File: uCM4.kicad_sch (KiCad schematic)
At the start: 63 parts, among them J1 UART, J10 Conn_01x04, J11 GPS, J2 Micro_SD_Card_Det, J3 I2C1, J4 USB_B_Micro, J5 DummyJ, J6 DummyJ, J7 SolderJumper_2_Open, J8 Camera 0, J9 Camera 1, SW1 SW_DIP_x01, SW2 SW_DIP_x01, SW3 SW_Push, SW4 SW_Push, U1 BNO055, U18 RT9742GGJ5, U2 SN74LVC1G07DBVR, U3 TPD4EUSB30DQAR, U4 TPS61022

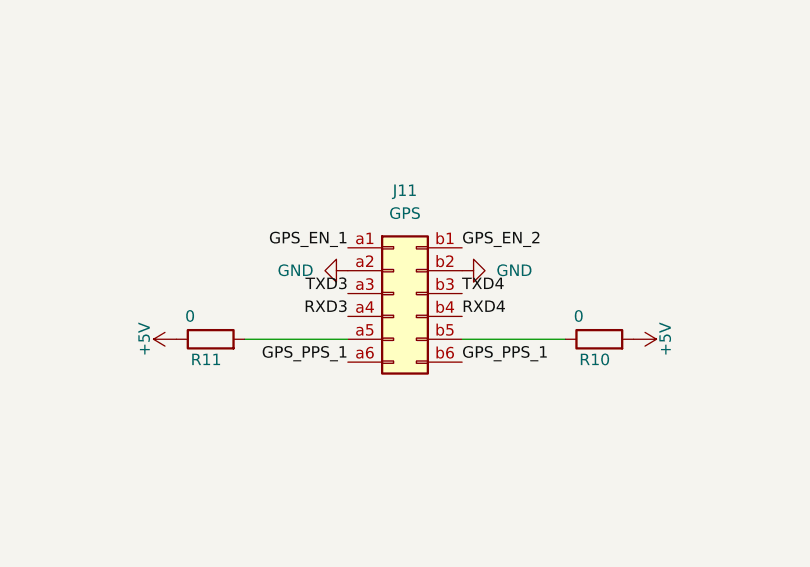
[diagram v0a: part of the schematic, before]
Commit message: Adding 3d models and arranging board
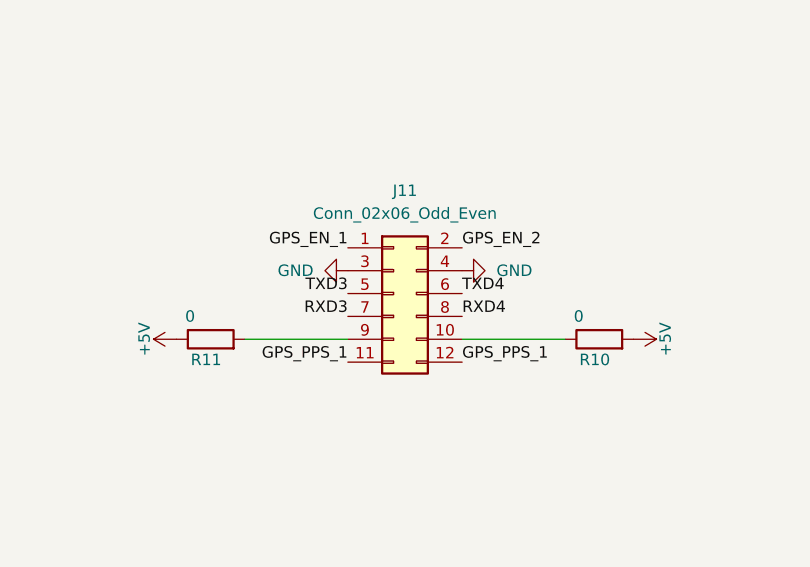
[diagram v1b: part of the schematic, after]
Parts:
- removed J11: GPS, symbol Connector_Generic:Conn_02x06_Row_Letter_First
- added J11: Conn_02x06_Odd_Even, Connector_PinHeader_2.54mm:PinHeader_2x06_P2.54mm_Vertical, symbol Connector_Generic:Conn_02x06_Odd_Even
- L1: footprint (none) -> CM4:XAL7030102MEC
- R19: footprint (none) -> Resistor_SMD:R_0603_1608Metric
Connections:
- net GND: now also J11.3 (Pin_3), J11.4 (Pin_4)
- net GPS_EN_1: now also J11.1 (Pin_1)
- net GPS_EN_2: now also J11.2 (Pin_2)
- net GPS_PPS_1: now also J11.11 (Pin_11), J11.12 (Pin_12)
- net RXD3: now also J11.7 (Pin_7)
- net RXD4: now also J11.8 (Pin_8)
- net TXD3: now also J11.5 (Pin_5)
- net TXD4: now also J11.6 (Pin_6)
- net at R11.2: now also J11.9 (Pin_9)
- net at R10.1: now also J11.10 (Pin_10)
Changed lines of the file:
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@@
 	)
 	(symbol
+		(lib_id "Connector_Generic:Conn_02x06_Odd_Even")
+		(at 162.56 64.77 0)
+		(unit 1)
+		(exclude_from_sim no)
+		(in_bom yes)
+		(on_board yes)
+		(dnp no)
+		(fields_autoplaced yes)
+		(property "Reference" "J11"
+			(at 163.83 53.34 0)
+			(effects
+				(font
+					(size 1.27 1.27)
+				)
+			)
+		)
+		(property "Value" "Conn_02x06_Odd_Even"
+			(at 163.83 55.88 0)
+			(effects
+				(font
+					(size 1.27 1.27)
+				)
+			)
+		)
+		(property "Footprint" "Connector_PinHeader_2.54mm:PinHeader_2x06_P2.54mm_Vertical"
+			(at 162.56 64.77 0)
+			(effects
+				(font
+					(size 1.27 1.27)
+				)
+				(hide yes)
+			)
+		)
+		(property "Datasheet" "~"
+			(at 162.56 64.77 0)
+			(effects
+				(font
+					(size 1.27 1.27)
+				)
+				(hide yes)
+			)
+		)
+		(property "Description" "Generic connector, double row, 02x06, odd/even pin numbering scheme (row 1 odd numbers, row 2 even numbers), script generated (kicad-library-utils/schlib/autogen/connector/)"
+			(at 162.56 64.77 0)
+			(effects
+				(font
+					(size 1.27 1.27)
+				)
+				(hide yes)
+			)
+		)
+		(pin "8"
+		)
+		(pin "5"
+		)
+		(pin "12"
+		)
+		(pin "4"
+		)
+		(pin "3"
+		)
+		(pin "1"
+		)
+		(pin "9"
+		)
+		(pin "6"
+		)
+		(pin "10"
+		)
+		(pin "7"
+		)
+		(pin "2"
+		)
+		(pin "11"
+		)
+		(instances
+			(project ""
+				(path "/ab308ddb-f5b4-4376-8062-4d719b3e690f"
+					(reference "J11")
+					(unit 1)
+				)
+			)
+		)
+	)
+	(symbol
 		(lib_id "power:GND")
 		(at 34.29 60.96 270)
@@
 			)
 		)
-		(property "Footprint" ""
+		(property "Footprint" "CM4:XAL7030102MEC"
 			(at 365.76 142.24 0)
 			(effects
@@
 			)
 		)
-		(property "Footprint" ""
+		(property "Footprint" "Resistor_SMD:R_0603_1608Metric"
 			(at 388.62 154.178 90)
 			(effects
@@
 					(unit 1)
 				)
-			)
-		)
-	)
-	(symbol
-		(lib_id "Connector_Generic:Conn_02x06_Row_Letter_First")
-		(at 162.56 64.77 0)
-		(unit 1)
-		(exclude_from_sim no)
-		(in_bom yes)
-		(on_board yes)
-		(dnp no)
-		(fields_autoplaced yes)
-		(property "Reference" "J11"
-			(at 163.83 53.34 0)
-			(effects
-				(font
-					(size 1.27 1.27)
-				)
-			)
-		)
-		(property "Value" "GPS"
-			(at 163.83 55.88 0)
-			(effects
-				(font
-					(size 1.27 1.27)
-				)
-			)
-		)
-		(property "Footprint" ""
-			(at 162.56 64.77 0)
-			(effects
-				(font
-					(size 1.27 1.27)
-				)
-				(hide yes)
-			)
-		)
-		(property "Datasheet" "~"
-			(at 162.56 64.77 0)
-			(effects
-				(font
-					(size 1.27 1.27)
-				)
-				(hide yes)
-			)
-		)
-		(property "Description" "Generic connector, double row, 02x06, row letter first pin numbering scheme (pin number consists of a letter for the row and a number for the pin index in this row. a1, ..., aN; b1, ..., bN), script generated (kicad-library-utils/schlib/autogen/connector/)"
-			(at 162.56 64.77 0)
-			(effects
-				(font
-					(size 1.27 1.27)
-				)
-				(hide yes)
-			)
-		)
-		(pin "b1"
-		)
-		(pin "a5"
-		)
-		(pin "a4"
-		)
-		(pin "a1"
-		)
-		(pin "a6"
-		)
-		(pin "b3"
-		)
-		(pin "b2"
-		)
-		(pin "b6"
-		)
-		(pin "b5"
-		)
-		(pin "a2"
-		)
-		(pin "b4"
-		)
-		(pin "a3"
-		)
-		(instances
-			(project ""
-				(path "/ab308ddb-f5b4-4376-8062-4d719b3e690f"
-					(reference "J11")
-					(unit 1)
-				)

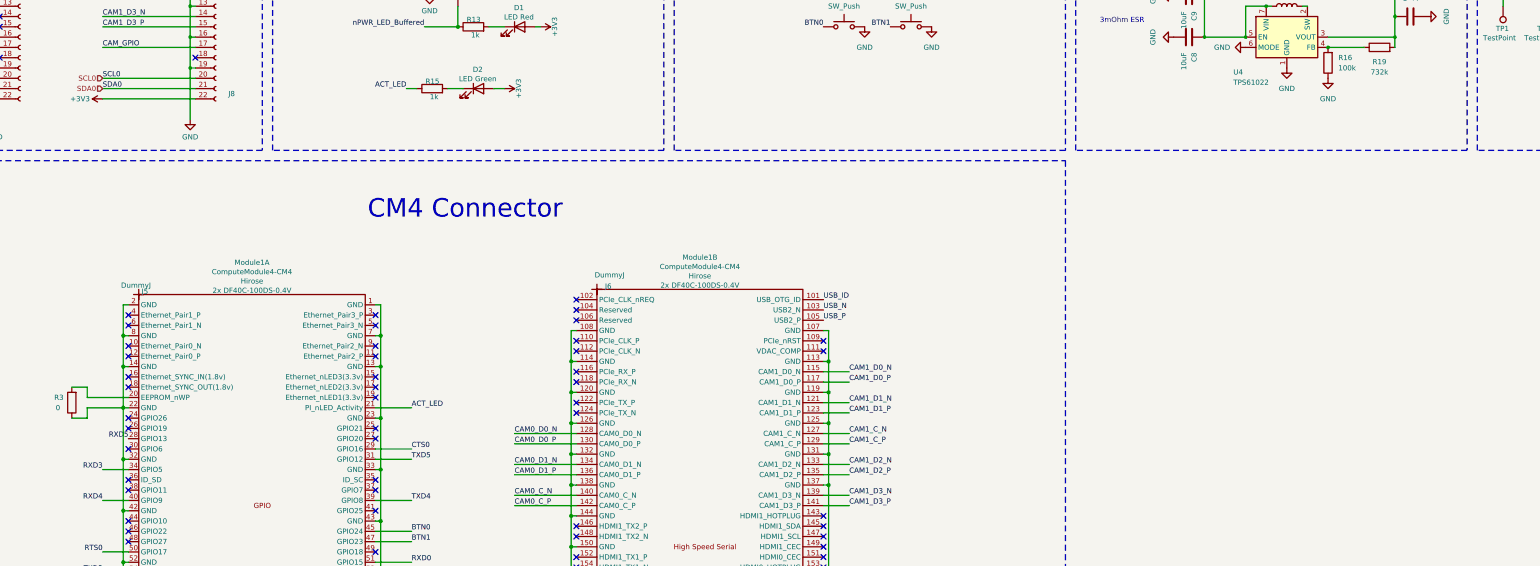
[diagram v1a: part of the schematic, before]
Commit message: Added environmental sensor.
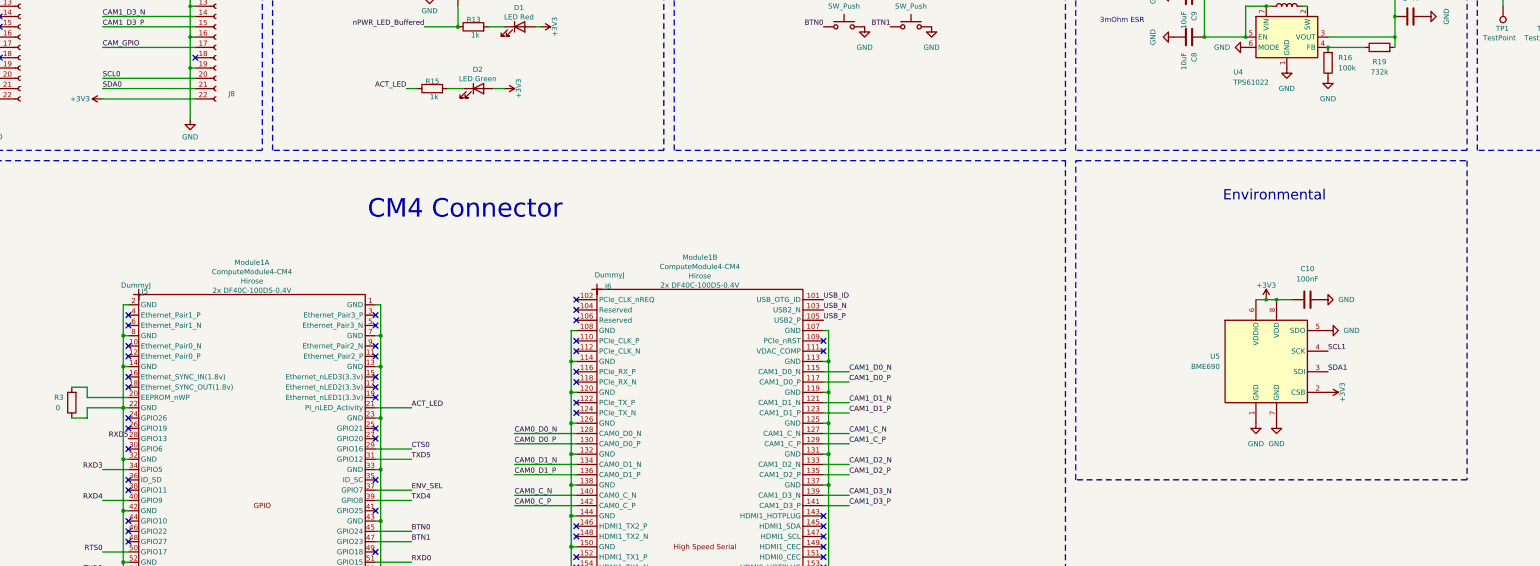
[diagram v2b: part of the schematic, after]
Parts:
- added C10: 100nF, Capacitor_SMD:C_0603_1608Metric, symbol Device:C
- added U5: BME690, Package_LGA:Bosch_LGA-8_3x3mm_P0.8mm_ClockwisePinNumbering, symbol Sensor:BME680
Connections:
- net +3V3: now also C10.1, U5.2 (CSB), U5.6 (VDDIO), U5.8 (VDD)
- net GND: now also C10.2, U5.1 (GND), U5.5 (SDO), U5.7 (GND)
- net SCL1: now also U5.4 (SCK)
- net SDA1: now also U5.3 (SDI)
- net ENV_SEL: now reaches Module1.37 (GPIO7)
- no-connect marks 100 -> 99
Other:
- note added: "Environmental"
